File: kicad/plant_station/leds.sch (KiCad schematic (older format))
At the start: 7 parts, among them J13 ZF5S-20-01-T-WT-TR, J14 505567-0471, J15 505567-0471

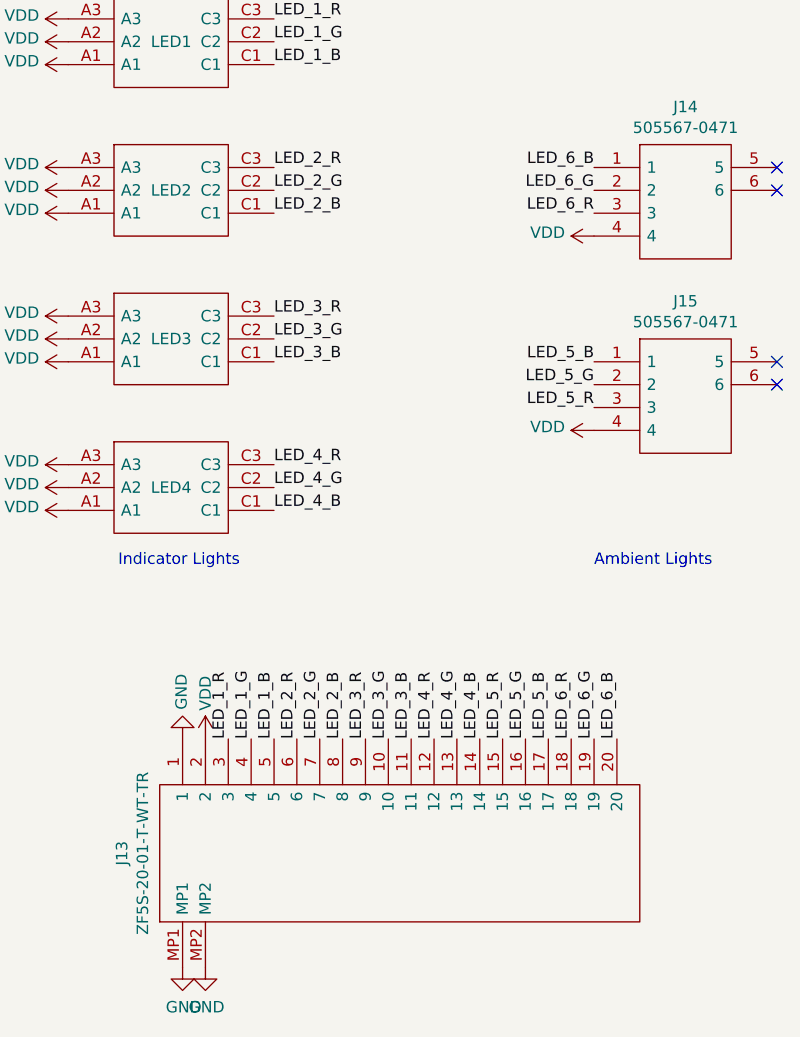
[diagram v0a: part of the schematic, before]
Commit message: v3 PCB in progress. Need to move LED driver to LEDs board and make it connect using the standard interface
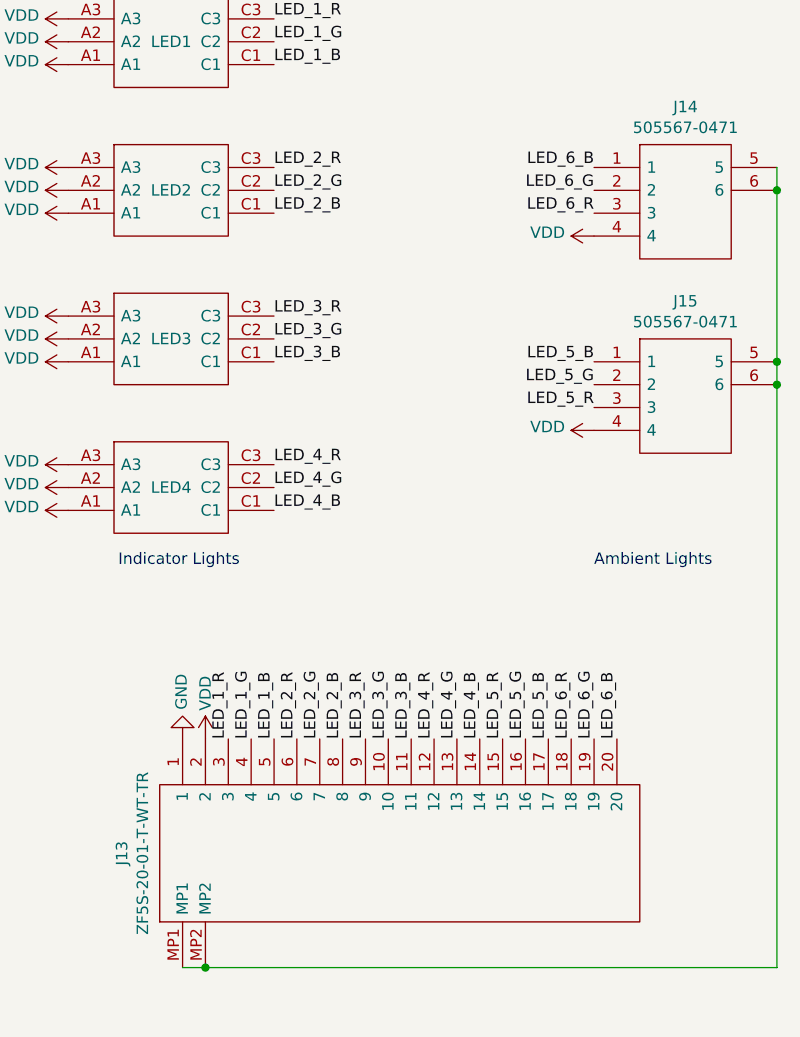
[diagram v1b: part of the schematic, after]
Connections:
- net GND: no longer J13.MP1, J13.MP2
- net at J14.5: now also J13.MP1, J13.MP2, J14.6, J15.5, J15.6
- no-connect marks 4 -> 0
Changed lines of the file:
@@
-$EndComp
-$Comp
-L power:GND #PWR054
-U 1 1 6022AA92
-P 3200 6000
-F 0 "#PWR054" H 3200 5750 50  0001 C CNN
-F 1 "GND" H 3205 5827 50  0000 C CNN
-F 2 "" H 3200 6000 50  0001 C CNN
-F 3 "" H 3200 6000 50  0001 C CNN
-	1    3200 6000
-	1    0    0    -1
-$EndComp
-$Comp
-L power:GND #PWR052
-U 1 1 6022AF44
-P 3100 6000
-F 0 "#PWR052" H 3100 5750 50  0001 C CNN
-F 1 "GND" H 3105 5827 50  0000 C CNN
-F 2 "" H 3100 6000 50  0001 C CNN
-F 3 "" H 3100 6000 50  0001 C CNN
-	1    3100 6000
-	1    0    0    -1
 $EndComp
 $Comp
@@
 	1    0    0    -1
 $EndComp
-NoConn ~ 5700 3350
-NoConn ~ 5700 3450
-NoConn ~ 5700 2500
-NoConn ~ 5700 2600
 $Comp
 L SamaSys:KRTBLSLPS1.32-VUVX-EQ+BTBV-D8+TWTZ-L1-B LED?
@@
 Text Label 3500 4000 0    50   ~ 0
 LED_4_B
-Text Label 4900 3550 2    50   ~ 0
-LED_5_R
-Text Label 4900 2700 2    50   ~ 0
-LED_6_R
 Text Label 4900 3450 2    50   ~ 0
 LED_5_G
-Text Label 4900 3350 2    50   ~ 0
-LED_5_B
 Text Label 4900 2600 2    50   ~ 0
 LED_6_G
-Text Label 4900 2500 2    50   ~ 0
-LED_6_B
 $Comp
 L power:VDD #PWR059
@@
 	1    0    0    -1
 $EndComp
+Text Label 4900 2500 2    50   ~ 0
+LED_6_B
+Text Label 4900 2700 2    50   ~ 0
+LED_6_R
+Text Label 4900 3350 2    50   ~ 0
+LED_5_B
+Text Label 4900 3550 2    50   ~ 0
+LED_5_R
+Wire Wire Line
+	3100 6000 3200 6000
+Wire Wire Line
+	5700 6000 5700 3450
+Connection ~ 3200 6000
+Wire Wire Line
+	3200 6000 5700 6000
+Connection ~ 5700 2600
+Wire Wire Line
+	5700 2600 5700 2500
+Connection ~ 5700 3350
+Wire Wire Line
+	5700 3350 5700 2600
+Connection ~ 5700 3450
+Wire Wire Line
+	5700 3450 5700 3350
 $EndSCHEMATC

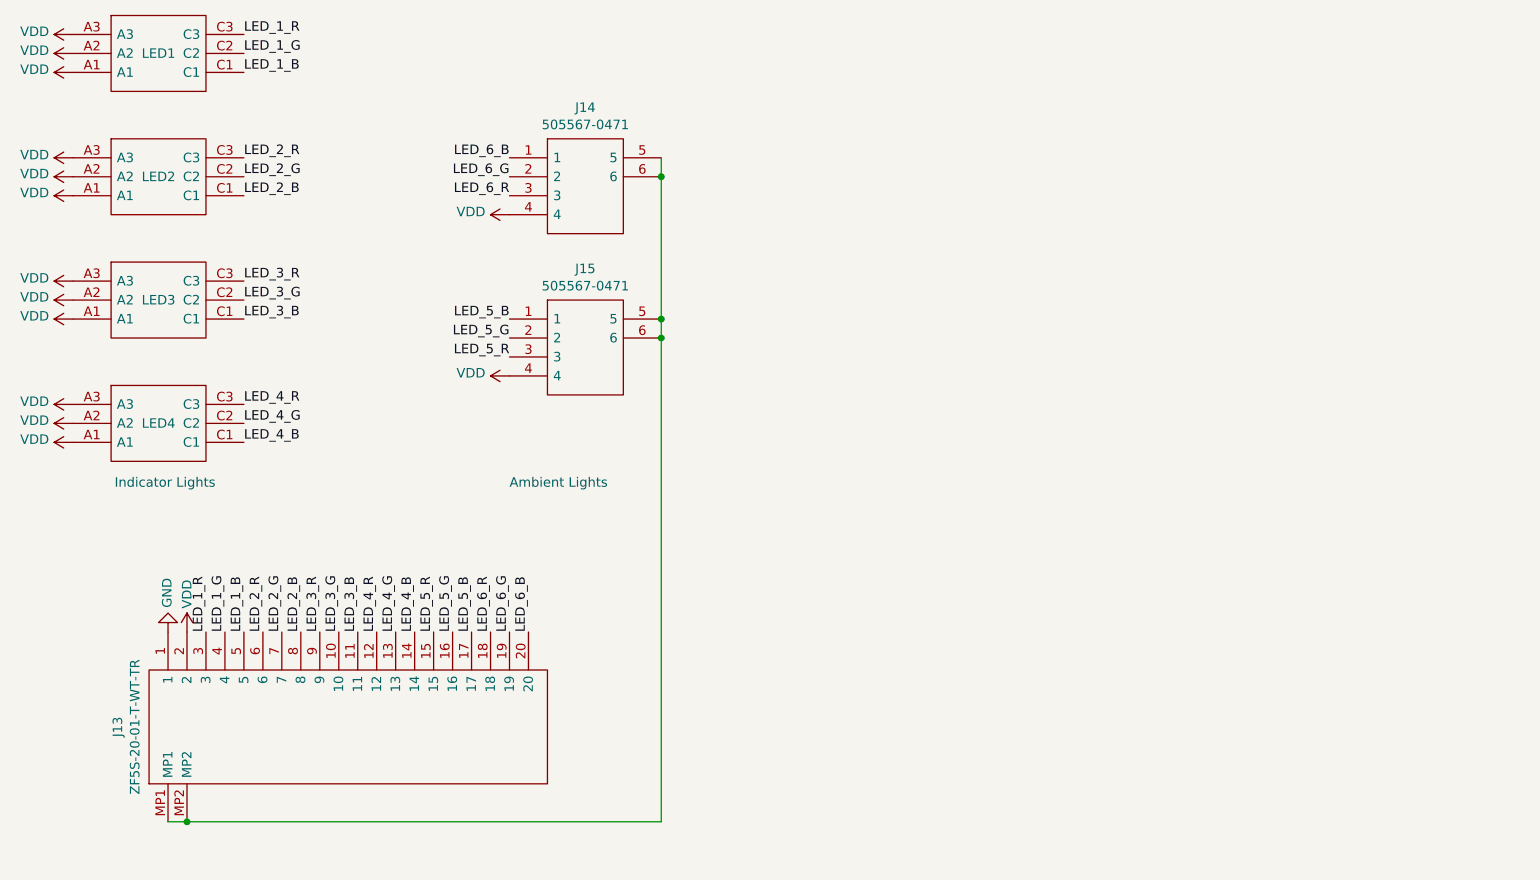
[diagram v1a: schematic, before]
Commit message: Moved the LED driver to LEDs board, refactored connectors. Hopefuly PCBNEW could update it all in place
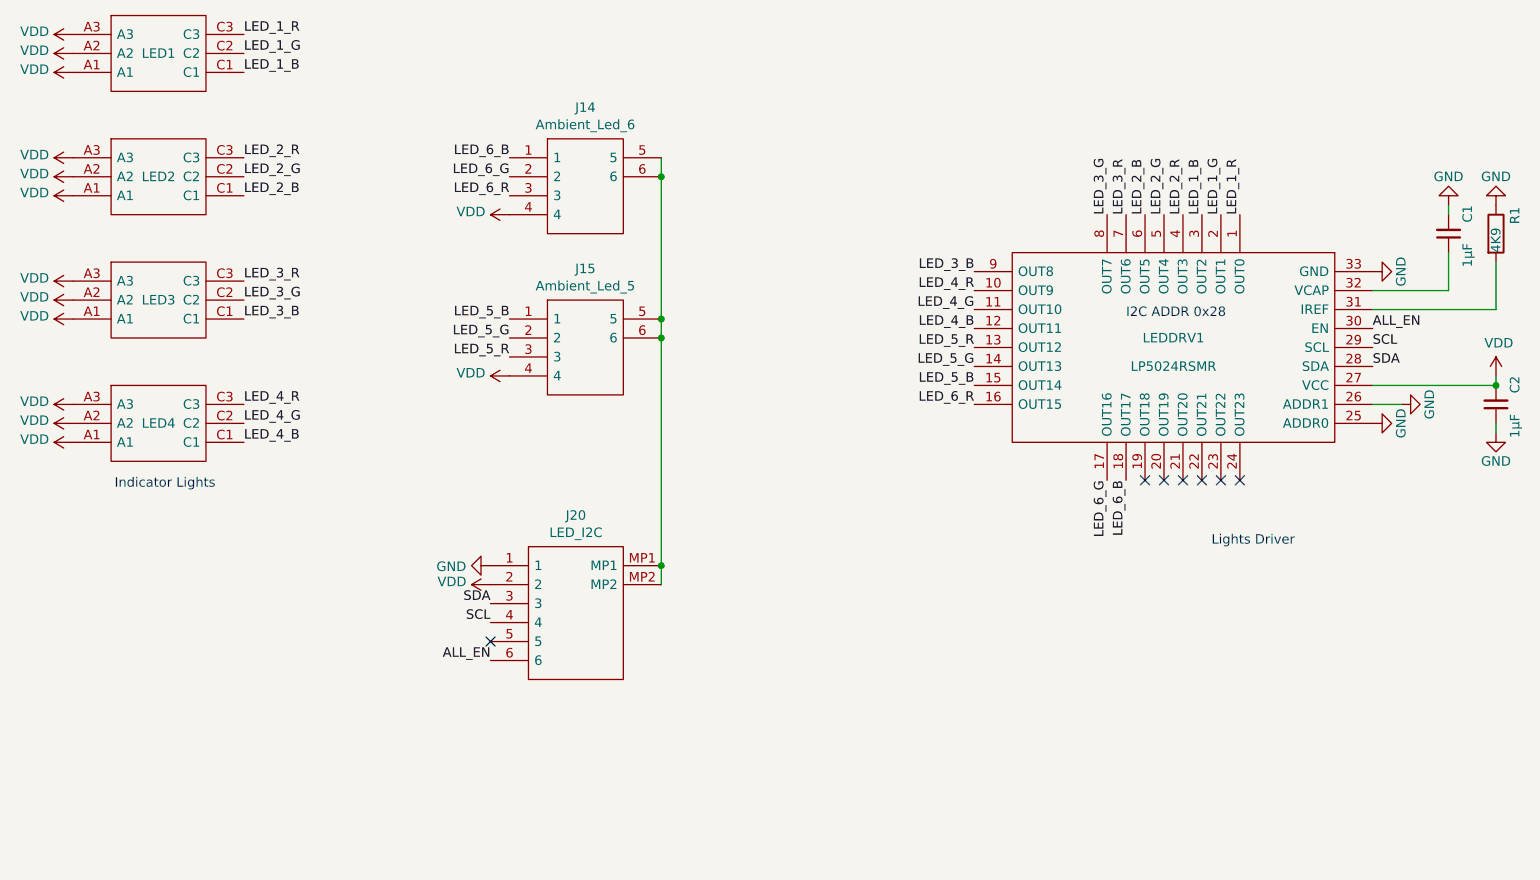
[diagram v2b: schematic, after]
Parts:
- removed J13: ZF5S-20-01-T-WT-TR, Parts:ZF5S2001TWTTR, symbol Parts:ZF5S-20-01-T-WT-TR
- added C1, C2: 1μF, Capacitor_SMD:C_1206_3216Metric, symbol Device:C_Small
- added J20: LED_I2C, Parts:Molex_Conn_SMD_01x06_505567_0671, symbol Parts:505567-0671
- added LEDDRV1: LP5024RSMR, SamacSys:QFN40P400X400X100-33N-D, symbol SamaSys:LP5024RSMR
- added R1: 4K9, Resistor_SMD:R_0805_2012Metric, symbol Device:R
- J14: value 505567-0471 -> Ambient_Led_6
- J15: value 505567-0471 -> Ambient_Led_5
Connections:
- net GND: now also C1.2, C2.1, J20.1, LEDDRV1.25 (ADDR0), LEDDRV1.26 (ADDR1), LEDDRV1.33 (GND), R1.1
- net LED_1_B: now also LEDDRV1.3 (OUT2)
- net LED_1_G: now also LEDDRV1.2 (OUT1)
- net LED_1_R: now also LEDDRV1.1 (OUT0)
- net LED_2_B: now also LEDDRV1.6 (OUT5)
- net LED_2_G: now also LEDDRV1.5 (OUT4)
- net LED_2_R: now also LEDDRV1.4 (OUT3)
- net LED_3_B: now also LEDDRV1.9 (OUT8)
- net LED_3_G: now also LEDDRV1.8 (OUT7)
- net LED_3_R: now also LEDDRV1.7 (OUT6)
- net LED_4_B: now also LEDDRV1.12 (OUT11)
- net LED_4_G: now also LEDDRV1.11 (OUT10)
- net LED_4_R: now also LEDDRV1.10 (OUT9)
- net LED_5_B: now also LEDDRV1.15 (OUT14)
- net LED_5_G: now also LEDDRV1.14 (OUT13)
- net LED_5_R: now also LEDDRV1.13 (OUT12)
- net LED_6_B: now also LEDDRV1.18 (OUT17)
- net LED_6_G: now also LEDDRV1.17 (OUT16)
- net LED_6_R: now also LEDDRV1.16 (OUT15)
- net VDD: now also C2.2, J20.2, LEDDRV1.27 (VCC)
- net at J14.5, J14.6, J15.5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: now also J20.MP1, J20.MP2
- new net: C1.1, LEDDRV1.32 (VCAP)
- new net: LEDDRV1.31 (IREF), R1.2
- new net ALL_EN: J20.6, LEDDRV1.30 (EN)
- new net SCL: J20.4, LEDDRV1.29 (SCL)
- new net SDA: J20.3, LEDDRV1.28 (SDA)
- no-connect marks 0 -> 7
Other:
- note added: "I2C ADDR 0x28"
- note added: "Lights Driver"
- note removed: "Ambient Lights"

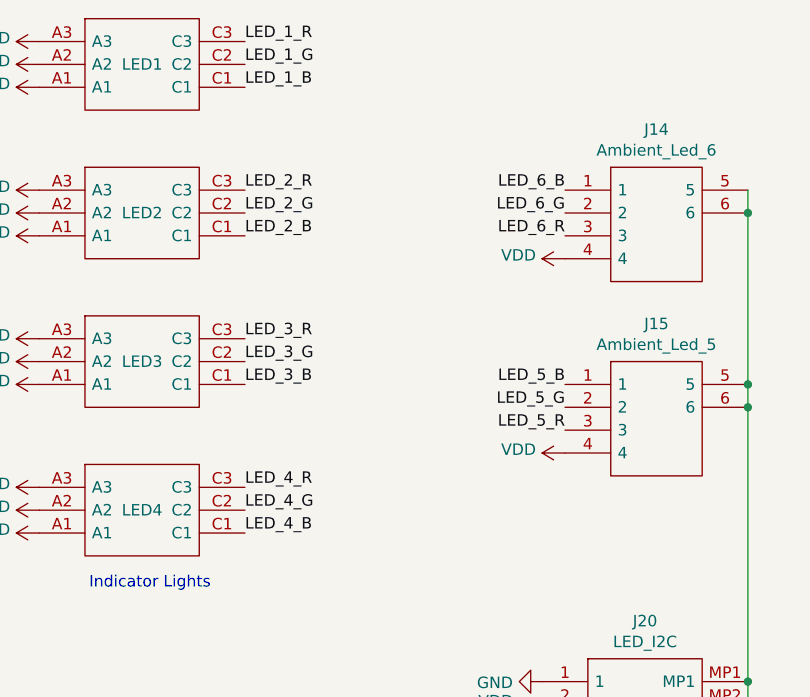
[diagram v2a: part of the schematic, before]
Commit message: LEDs board done via I2C bus
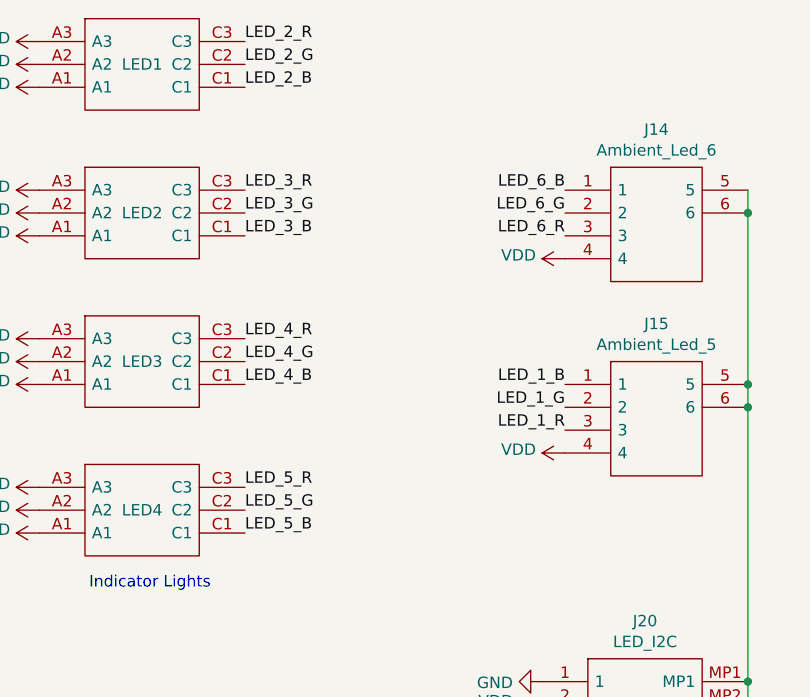
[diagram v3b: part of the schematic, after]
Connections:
- net LED_1_B: now also J15.1; no longer LED1.C1
- net LED_1_G: now also J15.2; no longer LED1.C2
- net LED_1_R: now also J15.3; no longer LED1.C3
- net LED_2_B: now also LED1.C1; no longer LED2.C1
- net LED_2_G: now also LED1.C2; no longer LED2.C2
- net LED_2_R: now also LED1.C3; no longer LED2.C3
- net LED_3_B: now also LED2.C1; no longer LED3.C1
- net LED_3_G: now also LED2.C2; no longer LED3.C2
- net LED_3_R: now also LED2.C3; no longer LED3.C3
- net LED_4_B: now also LED3.C1; no longer LED4.C1
- net LED_4_G: now also LED3.C2; no longer LED4.C2
- net LED_4_R: now also LED3.C3; no longer LED4.C3
- net LED_5_B: now also LED4.C1; no longer J15.1
- net LED_5_G: now also LED4.C2; no longer J15.2
- net LED_5_R: now also LED4.C3; no longer J15.3
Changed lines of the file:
@@
 $EndComp
 Text Label 3500 1850 0    50   ~ 0
-LED_1_R
-Text Label 3500 2500 0    50   ~ 0
 LED_2_R
 Text Label 3500 1950 0    50   ~ 0
-LED_1_G
-Text Label 3500 2600 0    50   ~ 0
 LED_2_G
 Text Label 3500 2050 0    50   ~ 0
-LED_1_B
-Text Label 3500 2700 0    50   ~ 0
 LED_2_B
 $Comp
@@
 	1    0    0    -1
 $EndComp
+Text Label 3500 2500 0    50   ~ 0
+LED_3_R
+Text Label 3500 2600 0    50   ~ 0
+LED_3_G
 Text Label 3500 3150 0    50   ~ 0
-LED_3_R
+LED_4_R
 Text Label 3500 3250 0    50   ~ 0
-LED_3_G
-Text Label 3500 3800 0    50   ~ 0
-LED_4_R
+LED_4_G
+Text Label 3500 2700 0    50   ~ 0
+LED_3_B
+Text Label 3500 3350 0    50   ~ 0
+LED_4_B
 Text Label 3500 3900 0    50   ~ 0
-LED_4_G
-Text Label 3500 3350 0    50   ~ 0
-LED_3_B
-Text Label 3500 4000 0    50   ~ 0
-LED_4_B
-Text Label 4900 3450 2    50   ~ 0
 LED_5_G
-Text Label 4900 2600 2    50   ~ 0
-LED_6_G
 $Comp
 L power:VDD #PWR059
@@
 	0    -1   -1   0
 $EndComp
-$Comp
-L power:VDD #PWR072
-U 1 1 5FA8F6B9
-P 4900 2800
-F 0 "#PWR072" H 4900 2650 50  0001 C CNN
-F 1 "VDD" V 4915 2927 50  0000 L CNN
-F 2 "" H 4900 2800 50  0001 C CNN
-F 3 "" H 4900 2800 50  0001 C CNN
-	1    4900 2800
-	0    -1   -1   0
-$EndComp
-Text Label 4900 2500 2    50   ~ 0
-LED_6_B
-Text Label 4900 2700 2    50   ~ 0
-LED_6_R
-Text Label 4900 3350 2    50   ~ 0
+Text Label 3500 4000 0    50   ~ 0
 LED_5_B
-Text Label 4900 3550 2    50   ~ 0
+Text Label 3500 3800 0    50   ~ 0
 LED_5_R
 Connection ~ 5700 2600
@@
 	5700 4650 5700 4750
 NoConn ~ 4800 5050
+$Comp
+L power:VDD #PWR072
+U 1 1 5FA8F6B9
+P 4900 2800
+F 0 "#PWR072" H 4900 2650 50  0001 C CNN
+F 1 "VDD" V 4915 2927 50  0000 L CNN
+F 2 "" H 4900 2800 50  0001 C CNN
+F 3 "" H 4900 2800 50  0001 C CNN
+	1    4900 2800
+	0    -1   -1   0
+$EndComp
+Text Label 4900 3350 2    50   ~ 0
+LED_1_B
+Text Label 4900 3450 2    50   ~ 0
+LED_1_G
+Text Label 4900 3550 2    50   ~ 0
+LED_1_R
+Text Label 4900 2600 2    50   ~ 0
+LED_6_G
+Text Label 4900 2500 2    50   ~ 0
+LED_6_B
+Text Label 4900 2700 2    50   ~ 0
+LED_6_R
 $EndSCHEMATC

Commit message: pcb v3 sent to production and the first attempts to design the enclosure
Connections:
- net LED_1_B: now also LED1.C1; no longer J15.1
- net LED_1_G: now also LED1.C2; no longer J15.2
- net LED_1_R: now also LED1.C3; no longer J15.3
- net LED_2_B: now also LED2.C1; no longer LED1.C1
- net LED_2_G: now also LED2.C2; no longer LED1.C2
- net LED_2_R: now also LED2.C3; no longer LED1.C3
- net LED_3_B: now also J14.1; no longer LED2.C1
- net LED_3_G: now also J14.2; no longer LED2.C2
- net LED_3_R: now also J14.3; no longer LED2.C3
- net LED_4_B: now also J15.1; no longer LED3.C1
- net LED_4_G: now also J15.2; no longer LED3.C2
- net LED_4_R: now also J15.3; no longer LED3.C3
- net LED_5_B: now also LED3.C1; no longer LED4.C1
- net LED_5_G: now also LED3.C2; no longer LED4.C2
- net LED_5_R: now also LED3.C3; no longer LED4.C3
- net LED_6_B: now also LED4.C1; no longer J14.1
- net LED_6_G: now also LED4.C2; no longer J14.2
- net LED_6_R: now also LED4.C3; no longer J14.3
- now unconnected: J14.5, J14.6, J15.5, J15.6, J20.MP1, J20.MP2
- no-connect marks 7 -> 13
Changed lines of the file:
@@
 	1    0    0    -1
 $EndComp
-Text Label 3500 1850 0    50   ~ 0
+Text Label 3500 2500 0    50   ~ 0
 LED_2_R
-Text Label 3500 1950 0    50   ~ 0
+Text Label 3500 2600 0    50   ~ 0
 LED_2_G
-Text Label 3500 2050 0    50   ~ 0
+Text Label 3500 2700 0    50   ~ 0
 LED_2_B
 $Comp
@@
 	1    0    0    -1
 $EndComp
-Text Label 3500 2500 0    50   ~ 0
+Text Label 4900 2700 2    50   ~ 0
 LED_3_R
-Text Label 3500 2600 0    50   ~ 0
+Text Label 4900 2600 2    50   ~ 0
 LED_3_G
-Text Label 3500 3150 0    50   ~ 0
+Text Label 4900 3550 2    50   ~ 0
 LED_4_R
+Text Label 4900 3450 2    50   ~ 0
+LED_4_G
+Text Label 4900 2500 2    50   ~ 0
+LED_3_B
+Text Label 4900 3350 2    50   ~ 0
+LED_4_B
 Text Label 3500 3250 0    50   ~ 0
-LED_4_G
-Text Label 3500 2700 0    50   ~ 0
-LED_3_B
-Text Label 3500 3350 0    50   ~ 0
-LED_4_B
-Text Label 3500 3900 0    50   ~ 0
 LED_5_G
 $Comp
@@
 	0    -1   -1   0
 $EndComp
-Text Label 3500 4000 0    50   ~ 0
+Text Label 3500 3350 0    50   ~ 0
 LED_5_B
-Text Label 3500 3800 0    50   ~ 0
+Text Label 3500 3150 0    50   ~ 0
 LED_5_R
-Connection ~ 5700 2600
-Wire Wire Line
-	5700 2600 5700 2500
-Connection ~ 5700 3350
-Wire Wire Line
-	5700 3350 5700 2600
-Wire Wire Line
-	5700 3450 5700 3350
 Text Label 9450 3600 0    50   ~ 0
 SDA
@@
 	0    -1   -1   0
 $EndComp
-Wire Wire Line
-	5700 3450 5700 4650
-Connection ~ 5700 3450
-Connection ~ 5700 4650
-Wire Wire Line
-	5700 4650 5700 4750
 NoConn ~ 4800 5050
 $Comp
@@
 	0    -1   -1   0
 $EndComp
-Text Label 4900 3350 2    50   ~ 0
+Text Label 3500 2050 0    50   ~ 0
 LED_1_B
-Text Label 4900 3450 2    50   ~ 0
+Text Label 3500 1950 0    50   ~ 0
 LED_1_G
-Text Label 4900 3550 2    50   ~ 0
+Text Label 3500 1850 0    50   ~ 0
 LED_1_R
-Text Label 4900 2600 2    50   ~ 0
+Text Label 3500 3900 0    50   ~ 0
 LED_6_G
-Text Label 4900 2500 2    50   ~ 0
+Text Label 3500 4000 0    50   ~ 0
 LED_6_B
-Text Label 4900 2700 2    50   ~ 0
+Text Label 3500 3800 0    50   ~ 0
 LED_6_R
+NoConn ~ 5700 2500
+NoConn ~ 5700 2600
+NoConn ~ 5700 3350
+NoConn ~ 5700 3450
+NoConn ~ 5700 4650
+NoConn ~ 5700 4750
 $EndSCHEMATC
